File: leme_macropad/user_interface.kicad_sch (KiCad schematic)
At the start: 29 parts, among them J2 OLED display, SW1 SW_Push, SW10 SW_Push, SW2 SW_Push, SW3 SW_Push, SW4 SW_Push, SW5 SW_Push, SW6 SW_Push, SW7 RotaryEncoder_Switch, SW9 SW_Push

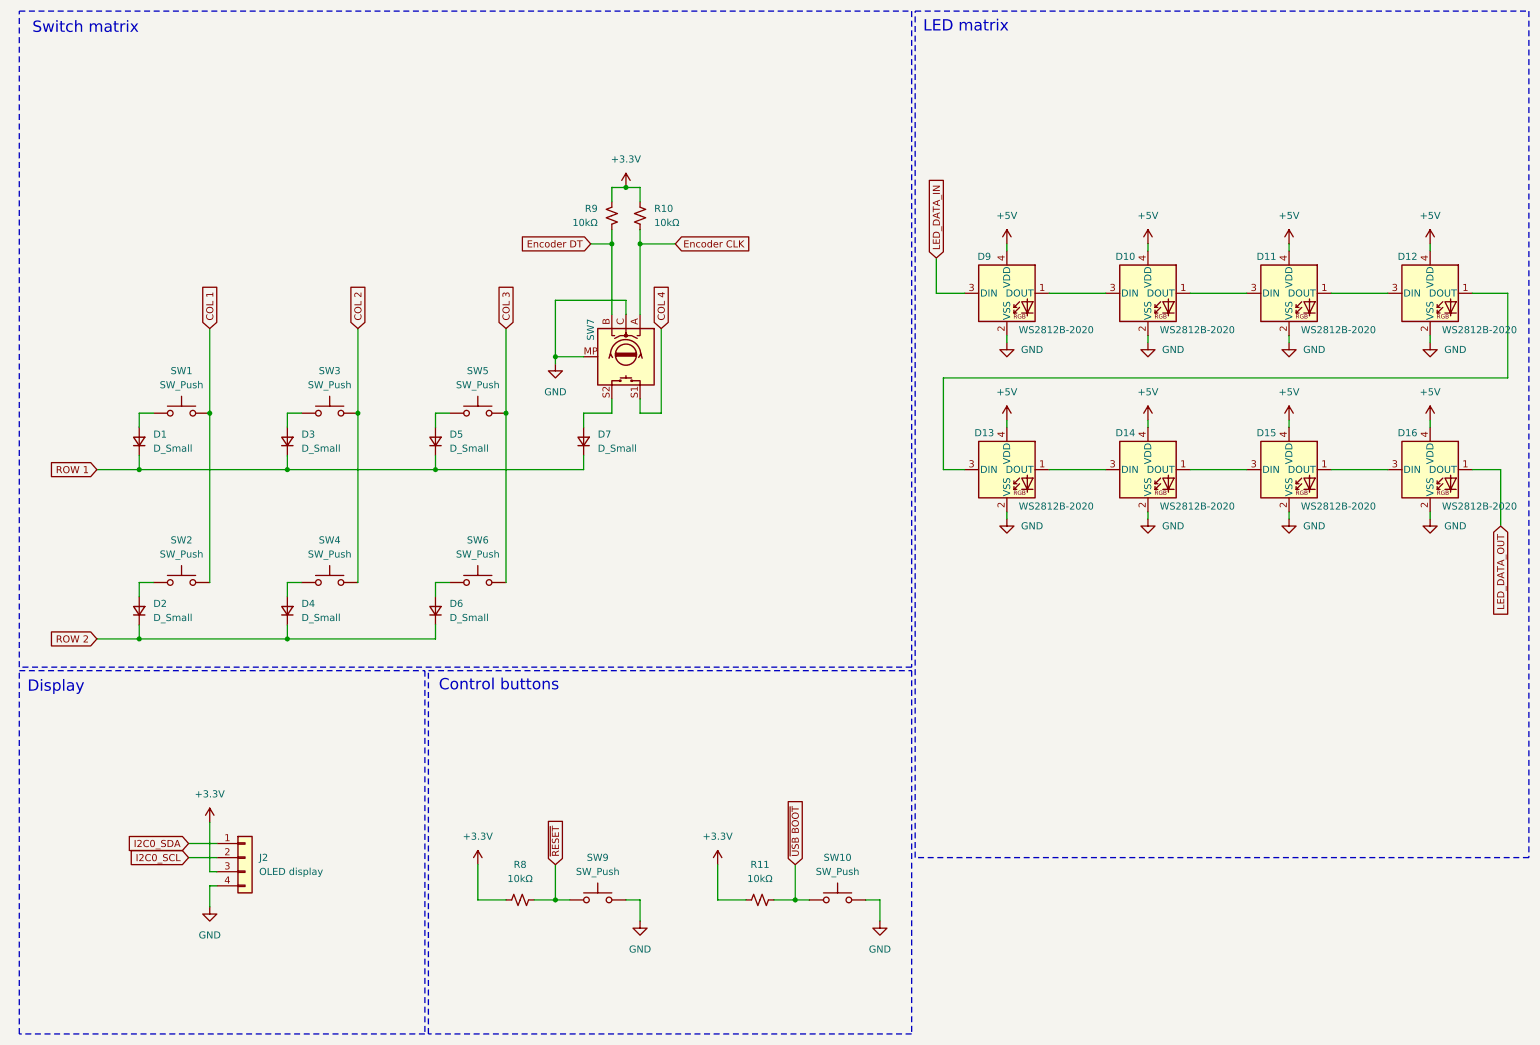
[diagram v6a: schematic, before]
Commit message: Reassigns designators based on component location on the PCB
Kicad 6 has a tool for that: geographical reannotate.
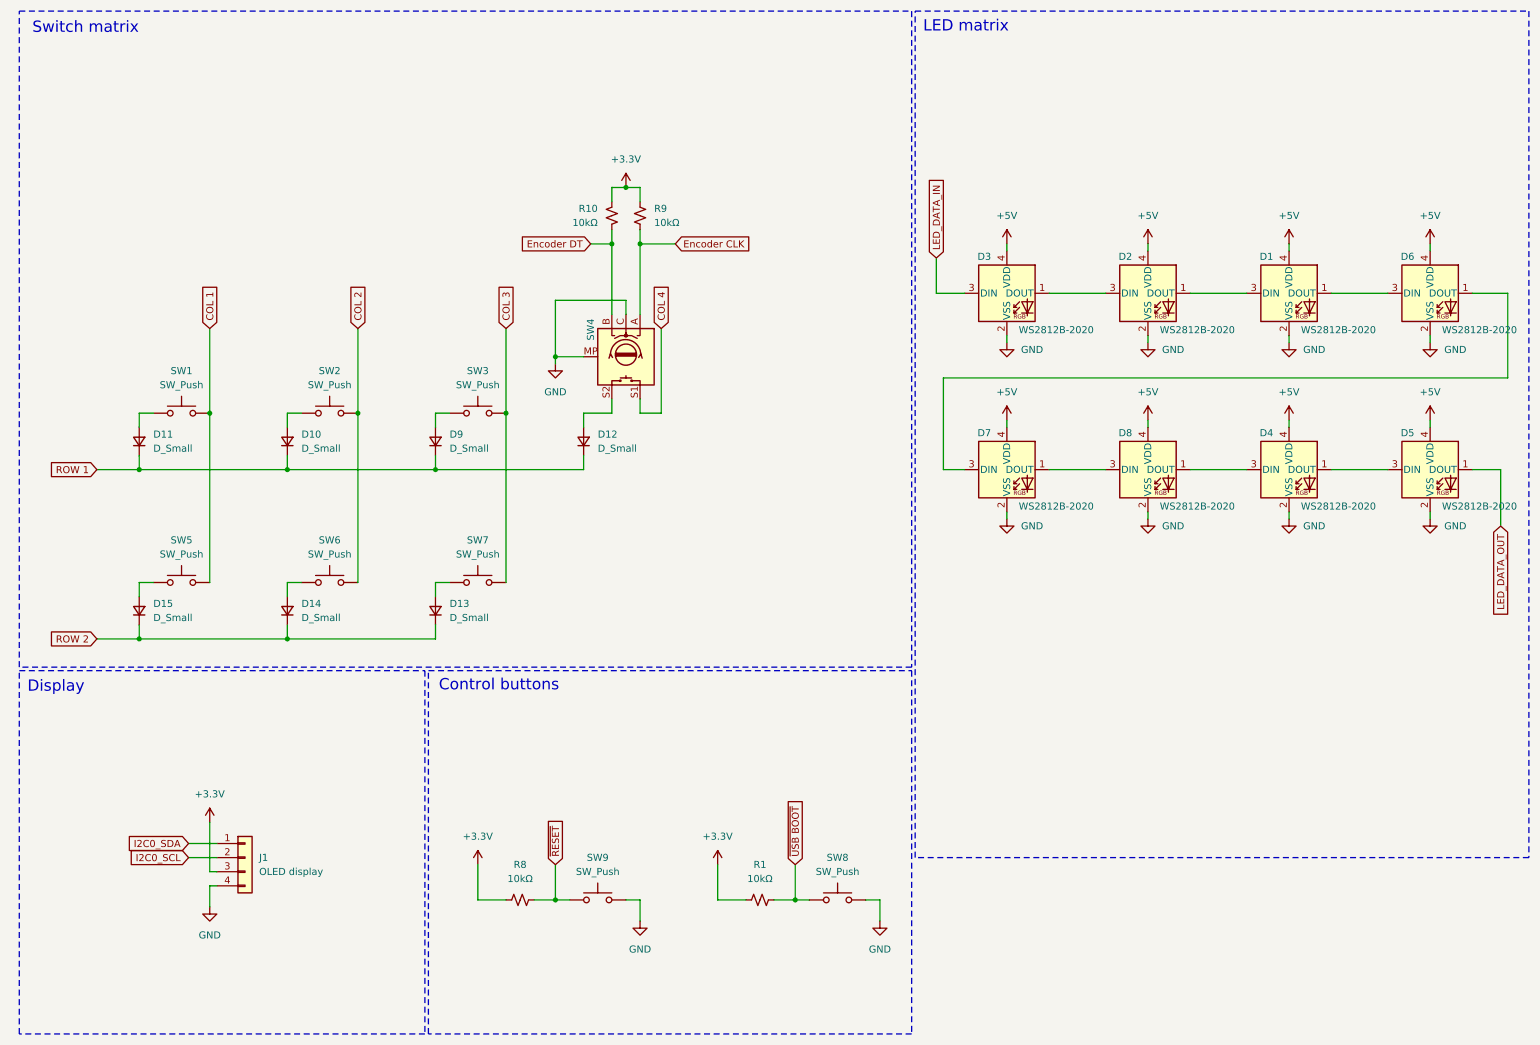
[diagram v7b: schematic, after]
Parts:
- renumbered D11 to D1, D3 to D10, D1 to D11, D7 to D12, D6 to D13, D4 to D14, D2 to D15, D10 to D2, D9 to D3, D15 to D4, D16 to D5, D12 to D6, D13 to D7, D14 to D8, D5 to D9, J2 to J1, R11 to R1, R9 to R10, R10 to R9, SW3 to SW2, SW5 to SW3, SW7 to SW4, SW2 to SW5, SW4 to SW6, SW6 to SW7, SW10 to SW8
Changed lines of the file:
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@@
 		(on_board yes)
 		(dnp no)
-		(property "Reference" "D14"
+		(property "Reference" "D8"
 			(at 211.836 88.646 0)
 			(effects
@@
 			(project "leme_macropad"
 				(path "/a37365a2-c635-4451-9354-78f9e753d687/b6fad1bd-9b8b-42cb-b41f-ac701051e19c"
-					(reference "D14")
+					(reference "D8")
 					(unit 1)
 				)
@@
 		(dnp no)
 		(fields_autoplaced yes)
-		(property "Reference" "SW10"
+		(property "Reference" "SW8"
 			(at 160.02 165.1 0)
 			(effects
@@
 			(project "leme_macropad"
 				(path "/a37365a2-c635-4451-9354-78f9e753d687/b6fad1bd-9b8b-42cb-b41f-ac701051e19c"
-					(reference "SW10")
+					(reference "SW8")
 					(unit 1)
 				)
@@
 		(on_board yes)
 		(dnp no)
-		(property "Reference" "D9"
+		(property "Reference" "D3"
 			(at 186.436 56.896 0)
 			(effects
@@
 			(project ""
 				(path "/a37365a2-c635-4451-9354-78f9e753d687/b6fad1bd-9b8b-42cb-b41f-ac701051e19c"
-					(reference "D9")
+					(reference "D3")
 					(unit 1)
 				)
@@
 		(on_board yes)
 		(dnp no)
-		(property "Reference" "D12"
+		(property "Reference" "D6"
 			(at 262.636 56.896 0)
 			(effects
@@
 			(project "leme_macropad"
 				(path "/a37365a2-c635-4451-9354-78f9e753d687/b6fad1bd-9b8b-42cb-b41f-ac701051e19c"
-					(reference "D12")
+					(reference "D6")
 					(unit 1)
 				)
@@
 		(dnp no)
 		(fields_autoplaced yes)
-		(property "Reference" "D5"
+		(property "Reference" "D9"
 			(at 90.17 88.8999 90)
 			(effects
@@
 			(project "leme_macropad"
 				(path "/a37365a2-c635-4451-9354-78f9e753d687/b6fad1bd-9b8b-42cb-b41f-ac701051e19c"
-					(reference "D5")
+					(reference "D9")
 					(unit 1)
 				)
@@
 		(on_board yes)
 		(dnp no)
-		(property "Reference" "D16"
+		(property "Reference" "D5"
 			(at 262.636 88.646 0)
 			(effects
@@
 			(project "leme_macropad"
 				(path "/a37365a2-c635-4451-9354-78f9e753d687/b6fad1bd-9b8b-42cb-b41f-ac701051e19c"
-					(reference "D16")
+					(reference "D5")
 					(unit 1)
 				)
@@
 		(dnp no)
 		(fields_autoplaced yes)
-		(property "Reference" "D3"
+		(property "Reference" "D10"
 			(at 63.5 88.8999 90)
 			(effects
@@
 			(project "leme_macropad"
 				(path "/a37365a2-c635-4451-9354-78f9e753d687/b6fad1bd-9b8b-42cb-b41f-ac701051e19c"
-					(reference "D3")
+					(reference "D10")
 					(unit 1)
 				)
@@
 		(dnp no)
 		(fields_autoplaced yes)
-		(property "Reference" "D2"
+		(property "Reference" "D15"
 			(at 36.83 119.3799 90)
 			(effects
@@
 			(project "leme_macropad"
 				(path "/a37365a2-c635-4451-9354-78f9e753d687/b6fad1bd-9b8b-42cb-b41f-ac701051e19c"
-					(reference "D2")
+					(reference "D15")
 					(unit 1)
 				)
@@
 		(on_board yes)
 		(dnp no)
-		(property "Reference" "D13"
+		(property "Reference" "D7"
 			(at 186.436 88.646 0)
 			(effects
@@
 			(project "leme_macropad"
 				(path "/a37365a2-c635-4451-9354-78f9e753d687/b6fad1bd-9b8b-42cb-b41f-ac701051e19c"
-					(reference "D13")
+					(reference "D7")
 					(unit 1)
 				)
@@
 		(dnp no)
 		(fields_autoplaced yes)
-		(property "Reference" "R10"
+		(property "Reference" "R9"
 			(at 127 48.2599 0)
 			(effects
@@
 			(project "leme_macropad"
 				(path "/a37365a2-c635-4451-9354-78f9e753d687/b6fad1bd-9b8b-42cb-b41f-ac701051e19c"
-					(reference "R10")
+					(reference "R9")
 					(unit 1)
 				)
@@
 		(on_board yes)
 		(dnp no)
-		(property "Reference" "D10"
+		(property "Reference" "D2"
 			(at 211.836 56.896 0)
 			(effects
@@
 			(project "leme_macropad"
 				(path "/a37365a2-c635-4451-9354-78f9e753d687/b6fad1bd-9b8b-42cb-b41f-ac701051e19c"
-					(reference "D10")
+					(reference "D2")
 					(unit 1)
 				)
@@
 		(on_board yes)
 		(dnp no)
-		(property "Reference" "D11"
+		(property "Reference" "D1"
 			(at 237.236 56.896 0)
 			(effects
@@
 			(project "leme_macropad"
 				(path "/a37365a2-c635-4451-9354-78f9e753d687/b6fad1bd-9b8b-42cb-b41f-ac701051e19c"
-					(reference "D11")
+					(reference "D1")
 					(unit 1)
 				)
@@
 		(dnp no)
 		(fields_autoplaced yes)
-		(property "Reference" "R11"
+		(property "Reference" "R1"
 			(at 146.05 166.37 90)
 			(effects
@@
 			(project "leme_macropad"
 				(path "/a37365a2-c635-4451-9354-78f9e753d687/b6fad1bd-9b8b-42cb-b41f-ac701051e19c"
-					(reference "R11")
+					(reference "R1")
 					(unit 1)
 				)
@@
 		(on_board yes)
 		(dnp no)
-		(property "Reference" "D15"
+		(property "Reference" "D4"
 			(at 237.236 88.646 0)
 			(effects
@@
 			(project "leme_macropad"
 				(path "/a37365a2-c635-4451-9354-78f9e753d687/b6fad1bd-9b8b-42cb-b41f-ac701051e19c"
-					(reference "D15")
+					(reference "D4")
 					(unit 1)
 				)
@@
 		(on_board yes)
 		(dnp no)
-		(property "Reference" "SW7"
+		(property "Reference" "SW4"
 			(at 115.57 68.072 0)
 			(effects
@@
 			(project "leme_macropad"
 				(path "/a37365a2-c635-4451-9354-78f9e753d687/b6fad1bd-9b8b-42cb-b41f-ac701051e19c"
-					(reference "SW7")
+					(reference "SW4")
 					(unit 1)
 				)
@@
 		(dnp no)
 		(fields_autoplaced yes)
-		(property "Reference" "D7"
+		(property "Reference" "D12"
 			(at 116.84 88.8999 90)
 			(effects
@@
 			(project "leme_macropad"
 				(path "/a37365a2-c635-4451-9354-78f9e753d687/b6fad1bd-9b8b-42cb-b41f-ac701051e19c"
-					(reference "D7")
+					(reference "D12")
 					(unit 1)
 				)
@@
 		(dnp no)
 		(fields_autoplaced yes)
-		(property "Reference" "SW2"
+		(property "Reference" "SW5"
 			(at 41.91 107.95 0)
 			(effects
@@
 			(project "leme_macropad"
 				(path "/a37365a2-c635-4451-9354-78f9e753d687/b6fad1bd-9b8b-42cb-b41f-ac701051e19c"
-					(reference "SW2")
+					(reference "SW5")
 					(unit 1)
 				)
@@
 		(dnp no)
 		(fields_autoplaced yes)
-		(property "Reference" "SW4"
+		(property "Reference" "SW6"
 			(at 68.58 107.95 0)
 			(effects
@@
 			(project "leme_macropad"
 				(path "/a37365a2-c635-4451-9354-78f9e753d687/b6fad1bd-9b8b-42cb-b41f-ac701051e19c"
-					(reference "SW4")
+					(reference "SW6")
 					(unit 1)
 				)
@@
 		(dnp no)
 		(fields_autoplaced yes)
-		(property "Reference" "SW5"
+		(property "Reference" "SW3"
 			(at 95.25 77.47 0)
 			(effects
@@
 			(project "leme_macropad"
 				(path "/a37365a2-c635-4451-9354-78f9e753d687/b6fad1bd-9b8b-42cb-b41f-ac701051e19c"
-					(reference "SW5")
+					(reference "SW3")
 					(unit 1)
 				)
@@
 		(dnp no)
 		(fields_autoplaced yes)
-		(property "Reference" "J2"
+		(property "Reference" "J1"
 			(at 55.88 165.0999 0)
 			(effects
@@
 			(project "leme_macropad"
 				(path "/a37365a2-c635-4451-9354-78f9e753d687/b6fad1bd-9b8b-42cb-b41f-ac701051e19c"
-					(reference "J2")
+					(reference "J1")
 					(unit 1)
 				)
@@
 		(dnp no)
 		(fields_autoplaced yes)
-		(property "Reference" "D1"
+		(property "Reference" "D11"
 			(at 36.83 88.8999 90)
 			(effects
@@
 			(project "leme_macropad"
 				(path "/a37365a2-c635-4451-9354-78f9e753d687/b6fad1bd-9b8b-42cb-b41f-ac701051e19c"
-					(reference "D1")
+					(reference "D11")
 					(unit 1)
 				)
@@
 		(dnp no)
 		(fields_autoplaced yes)
-		(property "Reference" "D6"
+		(property "Reference" "D13"
 			(at 90.17 119.3799 90)
 			(effects
@@
 			(project "leme_macropad"
 				(path "/a37365a2-c635-4451-9354-78f9e753d687/b6fad1bd-9b8b-42cb-b41f-ac701051e19c"
-					(reference "D6")
+					(reference "D13")
 					(unit 1)
 				)
@@
 		(on_board yes)
 		(dnp no)
-		(property "Reference" "R9"
+		(property "Reference" "R10"
 			(at 116.84 48.2599 0)
 			(effects
@@
 			(project "leme_macropad"
 				(path "/a37365a2-c635-4451-9354-78f9e753d687/b6fad1bd-9b8b-42cb-b41f-ac701051e19c"
-					(reference "R9")
+					(reference "R10")
 					(unit 1)
 				)
@@
 		(dnp no)
 		(fields_autoplaced yes)
-		(property "Reference" "SW6"
+		(property "Reference" "SW7"
 			(at 95.25 107.95 0)
 			(effects
@@
 			(project "leme_macropad"
 				(path "/a37365a2-c635-4451-9354-78f9e753d687/b6fad1bd-9b8b-42cb-b41f-ac701051e19c"
-					(reference "SW6")
+					(reference "SW7")
 					(unit 1)
 				)
@@
 		(dnp no)
 		(fields_autoplaced yes)
-		(property "Reference" "D4"
+		(property "Reference" "D14"
 			(at 63.5 119.3799 90)
 			(effects
@@
 			(project "leme_macropad"
 				(path "/a37365a2-c635-4451-9354-78f9e753d687/b6fad1bd-9b8b-42cb-b41f-ac701051e19c"
-					(reference "D4")
+					(reference "D14")
 					(unit 1)
 				)
@@
 		(dnp no)
 		(fields_autoplaced yes)
-		(property "Reference" "SW3"
+		(property "Reference" "SW2"
 			(at 68.58 77.47 0)
 			(effects
@@
 			(project "leme_macropad"
 				(path "/a37365a2-c635-4451-9354-78f9e753d687/b6fad1bd-9b8b-42cb-b41f-ac701051e19c"
-					(reference "SW3")
+					(reference "SW2")
 					(unit 1)
 				)

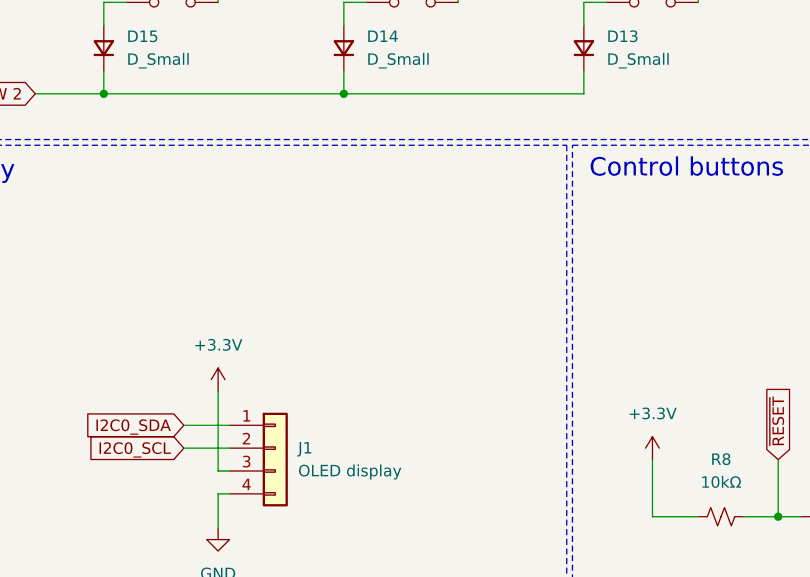
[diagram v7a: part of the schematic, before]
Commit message: Moves SDA/SCL i2c pins to make it easier to route
This also required moving the encoder pins, which will also make them
easier to route with this placement of the RP2040.

This commit also changes the configuration for QMK to use the new pins.
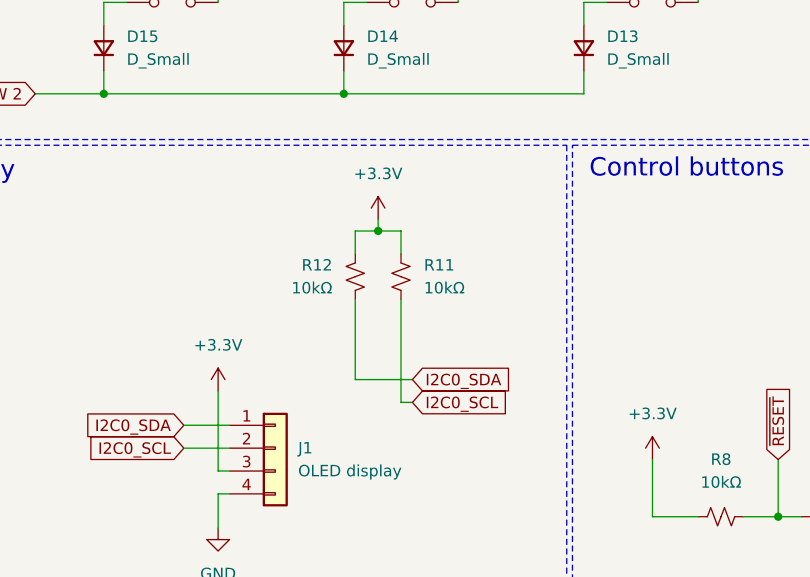
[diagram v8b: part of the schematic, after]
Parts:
- added R11, R12: 10kΩ, Resistor_SMD:R_0402_1005Metric_Pad0.72x0.64mm_HandSolder, symbol Device:R_Small_US
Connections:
- net +3.3V: now also R11.2, R12.2
- net I2C0_SCL: now also R11.1
- net I2C0_SDA: now also R12.1
